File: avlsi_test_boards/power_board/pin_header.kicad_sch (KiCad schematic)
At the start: 61 parts, among them J5 Conn_02x20_Odd_Even, J6 Conn_02x20_Odd_Even, J7 Conn_02x20_Odd_Even, J8 Conn_02x20_Odd_Even, U11 SN74LVC16T245DLR, U12 SN74LVC16T245DLR, U13 SN74LVC16T245DLR, U14 SN74LVC16T245DLR, U17 SN74LVC16T245DLR, U18 SN74LVC16T245DLR, U19 SN74LVC16T245DLR

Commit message: Fully routed
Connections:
- net VIN is gone; now on net V_Level_Shift: S1.A2, S1.B2, S2.A2, S2.B2, S3.A2, S3.B2, S4.A2, S4.B2, S5.A2, S5.B2, S6.A2, S6.B2, S7.A2, S7.B2
- net DGND: now also C10.1, C11.1, C12.1, C13.1, C14.1, C15.1, C16.1, C19.1, C20.1, C23.1, C24.1, C25.1, C26.1, C27.1, C28.1, C29.1, C30.1, C35.1, C36.1, C38.1, C39.1, C40.1, C41.1, C43.1, C44.1, C45.1, C6.1, C9.1, R1.2, R10.2, R11.2, R12.2, R13.2, R14.2, R2.2, R3.2, R4.2, R5.2, R6.2, R7.2, R8.2, R9.2, U11.10 (GND), U11.15 (GND), U11.21 (GND), U11.28 (GND), U11.34 (GND), U11.39 (GND), U11.4 (GND), U11.45 (GND), U12.10 (GND), U12.15 (GND), U12.21 (GND), U12.28 (GND), U12.34 (GND), U12.39 (GND), U12.4 (GND), U12.45 (GND), U13.10 (GND), U13.15 (GND), U13.21 (GND), U13.28 (GND), U13.34 (GND), U13.39 (GND), U13.4 (GND), U13.45 (GND), U14.10 (GND), U14.15 (GND), U14.21 (GND), U14.28 (GND), U14.34 (GND), U14.39 (GND), U14.4 (GND), U14.45 (GND), U17.10 (GND), U17.15 (GND), U17.21 (GND), U17.28 (GND), U17.34 (GND), U17.39 (GND), U17.4 (GND), U17.45 (GND), U18.10 (GND), U18.15 (GND), U18.21 (GND), U18.28 (GND), U18.34 (GND), U18.39 (GND), U18.4 (GND), U18.45 (GND), U19.10 (GND), U19.15 (GND), U19.21 (GND), U19.28 (GND), U19.34 (GND), U19.39 (GND), U19.4 (GND), U19.45 (GND)
- net DIR1_6: now also R4.1
- net HA1: now also J5.36 (Pin_36); no longer J5.35 (Pin_35)
- net HA10: now also J5.27 (Pin_27); no longer J5.28 (Pin_28)
- net HA11: now also J5.26 (Pin_26); no longer J5.25 (Pin_25)
- net HA12: now also J5.25 (Pin_25); no longer J5.26 (Pin_26)
- net HA13: now also J5.24 (Pin_24); no longer J5.23 (Pin_23)
- net HA14: now also J5.23 (Pin_23); no longer J5.24 (Pin_24)
- net HA15: now also J5.22 (Pin_22); no longer J5.21 (Pin_21)
- net HA16: now also J5.21 (Pin_21); no longer J5.22 (Pin_22)
- net HA2: now also J5.35 (Pin_35); no longer J5.36 (Pin_36)
- net HA3: now also J5.34 (Pin_34); no longer J5.33 (Pin_33)
- net HA4: now also J5.33 (Pin_33); no longer J5.34 (Pin_34)
- net HA5: now also J5.32 (Pin_32); no longer J5.31 (Pin_31)
- net HA6: now also J5.31 (Pin_31); no longer J5.32 (Pin_32)
- net HA7: now also J5.30 (Pin_30); no longer J5.29 (Pin_29)
- net HA8: now also J5.29 (Pin_29); no longer J5.30 (Pin_30)
- net HA9: now also J5.28 (Pin_28); no longer J5.27 (Pin_27)
- net HB1: now also J6.8 (Pin_8); no longer J6.7 (Pin_7)
- net HB11: now also J8.4 (Pin_4); no longer J8.3 (Pin_3)
- net HB12: now also J8.3 (Pin_3); no longer J8.4 (Pin_4)
- net HB13: now also J8.6 (Pin_6); no longer J8.5 (Pin_5)
- net HB14: now also J8.5 (Pin_5); no longer J8.6 (Pin_6)
- net HB15: now also J8.8 (Pin_8); no longer J8.7 (Pin_7)
- net HB16: now also J8.7 (Pin_7); no longer J8.8 (Pin_8)
- net HB2: now also J6.7 (Pin_7); no longer J6.8 (Pin_8)
- net HB3: now also J6.6 (Pin_6); no longer J6.5 (Pin_5)
- net HB4: now also J6.5 (Pin_5); no longer J6.6 (Pin_6)
- net HB5: now also J6.4 (Pin_4); no longer J6.3 (Pin_3)
- net HB6: now also J6.3 (Pin_3); no longer J6.4 (Pin_4)
- net HB7: now also J6.2 (Pin_2); no longer J6.1 (Pin_1)
- net HB8: now also J6.1 (Pin_1); no longer J6.2 (Pin_2)
- net HC6: now also U17.40 (1A6); no longer U17.39 (GND)
- net OPF1: now also J5.38 (Pin_38); no longer J5.37 (Pin_37)
- net OPH1: now also J5.37 (Pin_37); no longer J5.38 (Pin_38)
- net OPH2: now also J5.40 (Pin_40); no longer J5.39 (Pin_39)
- net OPH3: now also J5.39 (Pin_39); no longer J5.40 (Pin_40)
- removed net GND: C10.1, C11.1, C12.1, C13.1, C14.1, C15.1, C16.1, C19.1, C20.1, C23.1, C24.1, C25.1, C26.1, C27.1, C28.1, C29.1, C30.1, C35.1, C36.1, C38.1, C39.1, C40.1, C41.1, C43.1, C44.1, C45.1, C6.1, C9.1, R1.2, R10.2, R11.2, R12.2, R13.2, R14.2, R2.2, R3.2, R4.2, R5.2, R6.2, R7.2, R8.2, R9.2, U11.10 (GND), U11.15 (GND), U11.21 (GND), U11.28 (GND), U11.34 (GND), U11.39 (GND), U11.4 (GND), U11.45 (GND), U12.10 (GND), U12.15 (GND), U12.21 (GND), U12.28 (GND), U12.34 (GND), U12.39 (GND), U12.4 (GND), U12.45 (GND), U13.10 (GND), U13.15 (GND), U13.21 (GND), U13.28 (GND), U13.34 (GND), U13.39 (GND), U13.4 (GND), U13.45 (GND), U14.15 (GND), U14.21 (GND), U14.28 (GND), U14.34 (GND), U14.39 (GND), U14.4 (GND), U14.45 (GND), U17.15 (GND), U17.21 (GND), U17.28 (GND), U17.34 (GND), U17.4 (GND), U17.40 (1A6), U17.45 (GND), U18.10 (GND), U18.15 (GND), U18.21 (GND), U18.28 (GND), U18.34 (GND), U18.39 (GND), U18.4 (GND), U18.45 (GND), U19.10 (GND), U19.15 (GND), U19.21 (GND), U19.28 (GND), U19.34 (GND), U19.39 (GND), U19.4 (GND), U19.45 (GND)

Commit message: more changes
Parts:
- removed J7: Conn_02x20_Odd_Even, Connector_PinHeader_2.00mm:PinHeader_2x20_P2.00mm_Vertical, symbol Connector_Generic:Conn_02x20_Odd_Even
- added J4: Conn_02x10_Odd_Even, Connector_PinHeader_2.00mm:PinHeader_2x10_P2.00mm_Vertical, symbol Connector_Generic:Conn_02x10_Odd_Even
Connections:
- net 3VDD: now also J4.10 (Pin_10), J4.7 (Pin_7), J4.8 (Pin_8)
- net DGND: now also J4.1 (Pin_1), J4.15 (Pin_15), J4.2 (Pin_2), J4.3 (Pin_3), J4.4 (Pin_4), J4.6 (Pin_6), J4.9 (Pin_9)
- net FPGA_TCK: now also J4.11 (Pin_11)
- net FPGA_TDI: now also J4.13 (Pin_13)
- net FPGA_TDO: now also J4.5 (Pin_5)
- net FPGA_TMS: now also J4.14 (Pin_14)
- net OPB1: now also J4.20 (Pin_20)
- net OPD1: now also J4.19 (Pin_19)
- net SYS_CLK_MC2: now also J4.16 (Pin_16)
- net VCCBATT: now also J4.12 (Pin_12)
- net VCCO_MC2: now also J4.17 (Pin_17), J4.18 (Pin_18)

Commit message: Add partial changes
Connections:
- net DGND: now also U11.25 (*2OE), U11.48 (*1OE), U12.25 (*2OE), U12.48 (*1OE), U13.25 (*2OE), U13.48 (*1OE), U14.25 (*2OE), U17.25 (*2OE), U17.48 (*1OE), U18.25 (*2OE), U18.48 (*1OE), U19.25 (*2OE), U19.48 (*1OE)

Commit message: Add updated schematic
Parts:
- removed C10, C11, C12, C13, C14, C15, C16, C19, C20, C23, C24, C25, C26, C27, C28, C29, C30, C35, C36, C38, C39, C40, C41, C43, C44, C45, C6, C9: 1u, Capacitor_SMD:C_0603_1608Metric, symbol Device:C
- removed J4: Conn_02x10_Odd_Even, Connector_PinHeader_2.00mm:PinHeader_2x10_P2.00mm_Vertical, symbol Connector_Generic:Conn_02x10_Odd_Even
- removed R1, R10, R11, R12, R13, R14, R2, R3, R4, R5, R6, R7, R8, R9: 4.7k, Resistor_SMD:R_0201_0603Metric, symbol Device:R
- removed S1, S2, S3, S4, S5, S6, S7: 2454985-3, 24549853, symbol 2_DIP:2454985-3
- removed U11, U12, U13, U14, U17, U18, U19: SN74LVC16T245DLR, avlsi:DL48, symbol AVLSI:SN74LVC16T245DLR
- removed U2: ~, avlsi:opal_kelly_XEM7310_header, symbol AVLSI:opal_kelly_XEM7310_header
- added J7: Conn_02x20_Odd_Even, Connector_PinHeader_2.00mm:PinHeader_2x20_P2.00mm_Vertical, symbol Connector_Generic:Conn_02x20_Odd_Even
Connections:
- net 18VDD is gone; now on net FPGA_TCK: J5.6 (Pin_6)
- net HA1 is gone; now on net FPGA_33VDD: J5.36 (Pin_36)
- net HC7 is gone; now on net FPGA_GND: J8.16 (Pin_16)
- net HC8 is gone; now on net FPGA_33VDD: J8.15 (Pin_15)
- net HD14 is gone; now on net FPGA_GND: J8.37 (Pin_37)
- net HD16 is gone; now on net FPGA_GND: J8.39 (Pin_39)
- net HE13 is gone; now on net FPGA_GND: J6.37 (Pin_37)
- net HE15 is gone; now on net FPGA_GND: J6.39 (Pin_39)
- net HF7 is gone; now on net FPGA_GND: J6.15 (Pin_15)
- net HF8 is gone; now on net FPGA_33VDD: J6.16 (Pin_16)
- net FPGA_TDI: now also J5.10 (Pin_10)
- net FPGA_TDO: now also J5.7 (Pin_7)
- net FPGA_TMS: now also J5.8 (Pin_8)
- net SYS_CKL_MC1: now also J7.7 (Pin_7); no longer J5.13 (Pin_13)
- net SYS_CLK_MC2: now also J5.12 (Pin_12)
- net VCCBATT: now also J5.4 (Pin_4)
- net XADC_VN: now also J7.9 (Pin_9); no longer J5.14 (Pin_14)
- net XADC_VP: now also J7.11 (Pin_11); no longer J5.15 (Pin_15)
- net 10VDD renamed MC2_12
- net MC2_12: no longer J5.12 (Pin_12)
- net 33VDD renamed FPGA_33VDD
- net FPGA_33VDD: now also J5.1 (Pin_1), J7.10 (Pin_10), J7.12 (Pin_12), J7.14 (Pin_14), J7.35 (Pin_35); no longer J5.4 (Pin_4)
- removed net DGND: J5.1 (Pin_1), J5.10 (Pin_10), J5.16 (Pin_16), J5.19 (Pin_19), J5.2 (Pin_2), J5.20 (Pin_20)
- net HA10 renamed MC2_28_PIN
- net HA11 renamed MC2_25_PIN
- net HA12 renamed MC2_26_PIN
- net HA13 renamed MC2_23_PIN
- net HA14 renamed MC2_24
- net HA15 renamed MC2_21_PIN
- net HA16 renamed MC2_22
- net HA2 renamed FPGA_GND
- net FPGA_GND: now also J5.13 (Pin_13), J5.14 (Pin_14), J5.2 (Pin_2), J7.1 (Pin_1), J7.13 (Pin_13), J7.36 (Pin_36)
- net HA3 renamed MC2_33_PIN
- net HA4 renamed MC2_34_PIN
- net HA5 renamed MC2_31_PIN
- net HA6 renamed MC2_32_PIN
- net HA7 renamed MC2_29_PIN
- net HA8 renamed MC2_30_PIN
- net HA9 renamed MC2_27_PIN
- net HB1 renamed MC2_47_PIN
- net HB10 renamed MC1_42_PIN
- net HB11 renamed MC1_43_PIN
- net HB12 renamed MC1_44_PIN
- net HB13 renamed MC1_45_PIN
- net HB14 renamed MC1_46_PIN
- net HB15 renamed MC1_47_PIN
- net HB16 renamed MC1_48_PIN
- net HB2 renamed MC2_48_PIN
- net HB3 renamed MC2_45_PIN
- net HB4 renamed MC2_46_PIN
- net HB5 renamed MC2_43_PIN
- net HB6 renamed MC2_44_PIN
- net HB7 renamed MC2_41_PIN
- net HB8 renamed MC2_42_PIN
- net HB9 renamed MC1_41_PIN
- net HC1 renamed MC1_49_PIN
- net HC10 renamed MC1_58_PIN
- net HC11 renamed MC1_59_PIN
- net HC12 renamed MC1_60_PIN
- net HC13 renamed MC1_61_PIN
- net HC14 renamed MC1_62_PIN
- net HC15 renamed MC1_63_PIN
- net HC16 renamed MC1_64_PIN
- net HC2 renamed MC1_50_PIN
- net HC3 renamed MC1_51_PIN
- net HC4 renamed MC1_52_PIN
- net HC5 renamed MC1_53_PIN
- net HC6 renamed MC1_54_PIN
- net HC9 renamed MC1_57_PIN
- net HD1 renamed MC1_65_PIN
- net HD10 renamed MC1_74_PIN
- net HD11 renamed MC1_75
- net HD12 renamed MC1_76_PIN
- net HD13 renamed MC1_77
- net HD15 renamed MC1_79
- net HD2 renamed MC1_66_PIN
- net HD3 renamed MC1_67_PIN
- net HD4 renamed MC1_68_PIN
- net HD5 renamed MC1_69_PIN
- net HD6 renamed MC1_70_PIN
- net HD7 renamed MC1_71_PIN
- net HD8 renamed MC1_72_PIN
- net HD9 renamed MC1_73
- net HE1 renamed MC2_66_PIN
- net HE10 renamed MC2_73_PIN
- net HE11 renamed MC2_76_PIN
- net HE12 renamed MC2_75_PIN
- net HE14 renamed MC2_77_PIN
- net HE16 renamed MC2_79_PIN
- net HE2 renamed MC2_65_PIN
- net HE3 renamed MC2_68_PIN
- net HE4 renamed MC2_67_PIN
- net HE5 renamed MC2_70_PIN
- net HE6 renamed MC2_69_PIN
- net HE7 renamed MC2_72_PIN
- net HE8 renamed MC2_71_PIN
- net HE9 renamed MC2_74_PIN
- net HF1 renamed MC2_50_PIN
- net HF10 renamed MC2_57_PIN
- net HF11 renamed MC2_60_PIN
- net HF12 renamed MC2_59_PIN
- net HF13 renamed MC2_62_PIN
- net HF14 renamed MC2_61_PIN
- net HF15 renamed MC2_64_PIN
- net HF16 renamed MC2_63_PIN
- net HF2 renamed MC2_49_PIN
- net HF3 renamed MC2_52_PIN
- net HF4 renamed MC2_51_PIN
- net HF5 renamed MC2_54_PIN
- net HF6 renamed MC2_53_PIN
- net HF9 renamed MC2_58_PIN
- net OPF1 renamed MC2_37_PIN
- net OPH1 renamed MC2_38_PIN
- net OPH2 renamed MC2_39_PIN
- net OPH3 renamed MC2_40_PIN
- net VCCO_MC1 renamed MC2_17_PIN
- net MC2_17_PIN: no longer J5.17 (Pin_17)
- removed net VDCIN: J5.7 (Pin_7), J5.8 (Pin_8), J5.9 (Pin_9)
- new net FPGA_10VDD: J7.3 (Pin_3), J7.5 (Pin_5)
- new net FPGA_18VDD: J7.8 (Pin_8)
- new net FPGA_VCDIN: J7.2 (Pin_2), J7.4 (Pin_4), J7.6 (Pin_6)
- new net MC1_15_PIN: J7.16 (Pin_16)
- new net MC1_16_PIN: J7.15 (Pin_15)
- new net MC1_17_PIN: J7.18 (Pin_18)
- new net MC1_18_PIN: J7.17 (Pin_17)
- new net MC1_19_PIN: J7.20 (Pin_20)
- new net MC1_20_PIN: J7.19 (Pin_19)
- new net MC1_21_PIN: J7.22 (Pin_22)
- new net MC1_22_PIN: J7.21 (Pin_21)
- new net MC1_23_PIN: J7.24 (Pin_24)
- new net MC1_24_PIN: J7.23 (Pin_23)
- new net MC1_25_PIN: J7.26 (Pin_26)
- new net MC1_26_PIN: J7.25 (Pin_25)
- new net MC1_27_PIN: J7.28 (Pin_28)
- new net MC1_28_PIN: J7.27 (Pin_27)
- new net MC1_29_PIN: J7.30 (Pin_30)
- new net MC1_30_PIN: J7.29 (Pin_29)
- new net MC1_31_PIN: J7.32 (Pin_32)
- new net MC1_32_PIN: J7.31 (Pin_31)
- new net MC1_33_PIN: J7.34 (Pin_34)
- new net MC1_34_PIN: J7.33 (Pin_33)
- new net MC1_37_PIN: J7.38 (Pin_38)
- new net MC1_38_PIN: J7.37 (Pin_37)
- new net MC1_39_PIN: J7.40 (Pin_40)
- new net MC1_40_PIN: J7.39 (Pin_39)
- new net MC2_10_PIN: J5.9 (Pin_9)
- new net MC2_15_PIN: J5.16 (Pin_16)
- new net MC2_16: J5.15 (Pin_15)
- new net MC2_18: J5.17 (Pin_17)
- new net MC2_19_PIN: J5.20 (Pin_20)
- new net MC2_20: J5.19 (Pin_19)
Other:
- note removed: "1 extra pad"
- note removed: "3 extra pads"
- note removed: "Near analog power, empty pins are open"
- note removed: "On back copper"
- note removed: "This side up"
- moved on the sheet: J6

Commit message: Add fix typo
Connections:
- net SYS_CKL_MC1 renamed SYS_CLK_MC1
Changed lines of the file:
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@@
 		)
 	)
-	(global_label "SYS_CKL_MC1"
+	(global_label "SYS_CLK_MC1"
 		(shape input)
 		(at 222.25 40.64 180)

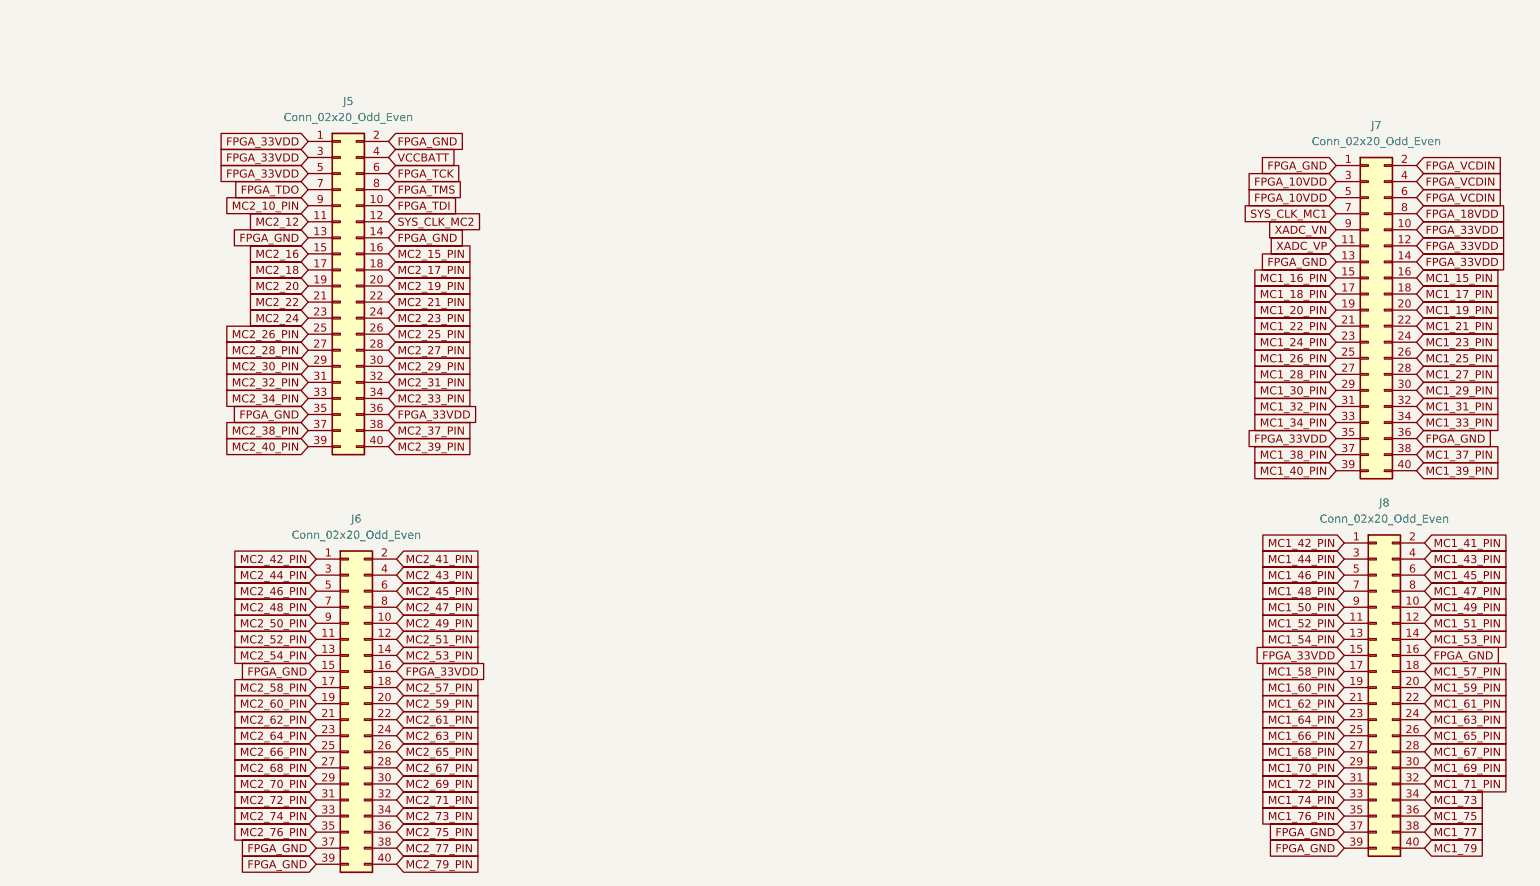
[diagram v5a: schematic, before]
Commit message: Update schematic and initial layout for pcb
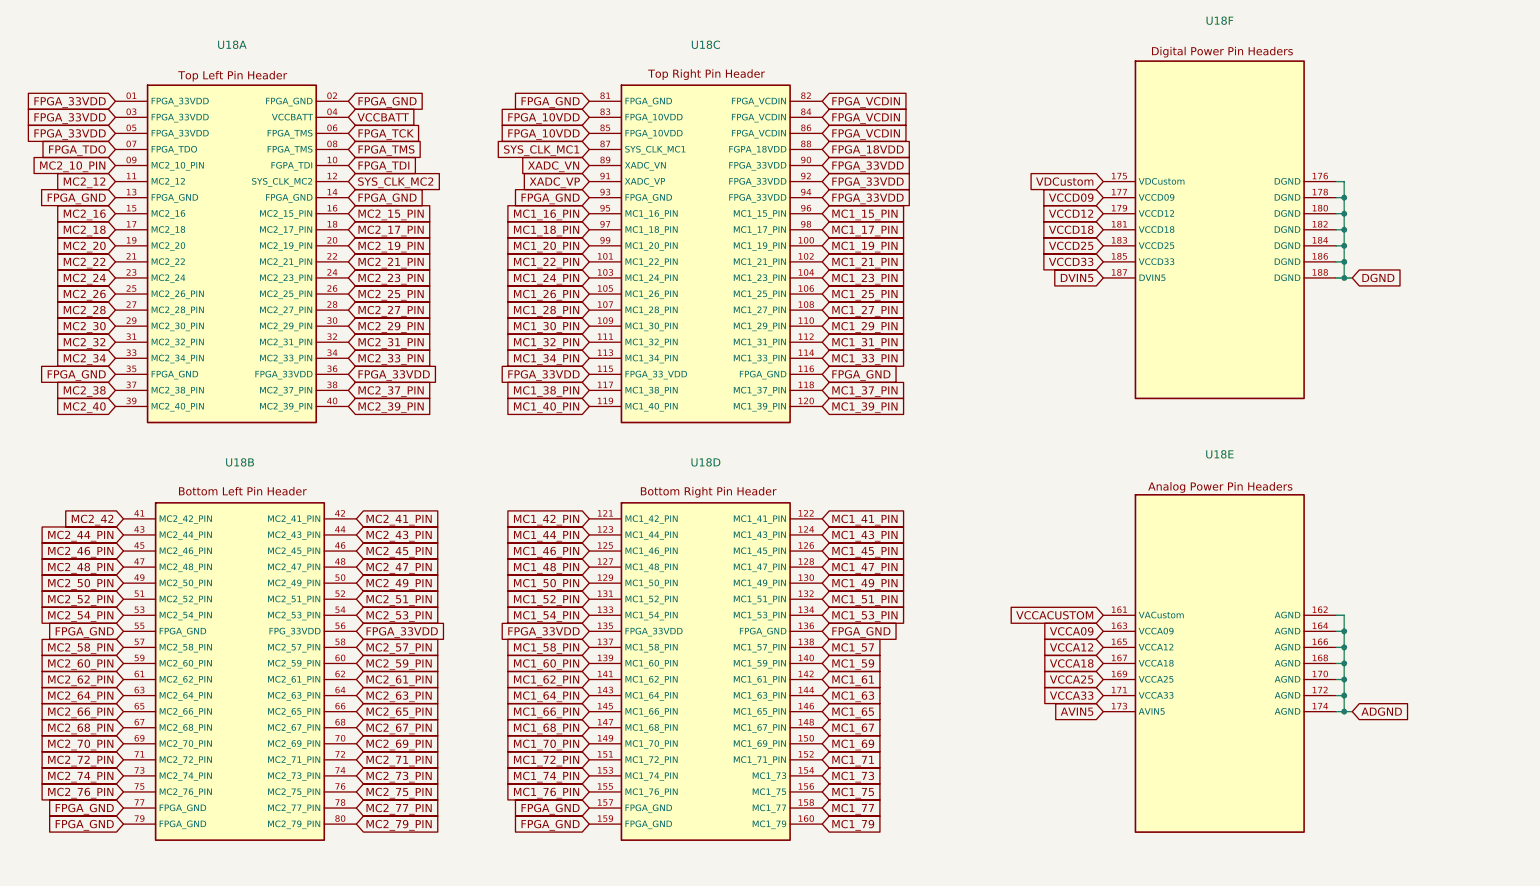
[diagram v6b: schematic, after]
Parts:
- removed J5, J6, J7, J8: Conn_02x20_Odd_Even, Connector_PinHeader_2.00mm:PinHeader_2x20_P2.00mm_Vertical, symbol Connector_Generic:Conn_02x20_Odd_Even
- added U18: ~, avlsi_preferred_parts:avlsi_power_board_opal_kelly, symbol avlsi_preferred_parts:avlsi_power_board_opal_kelly
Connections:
- net FPGA_10VDD: now also U18.83 (FPGA_10VDD), U18.85 (FPGA_10VDD)
- net FPGA_18VDD: now also U18.88 (FGPA_18VDD)
- net FPGA_33VDD: now also U18.01 (FPGA_33VDD), U18.03 (FPGA_33VDD), U18.05 (FPGA_33VDD), U18.115 (FPGA_33_VDD), U18.135 (FPGA_33VDD), U18.36 (FPGA_33VDD), U18.56 (FPG_33VDD), U18.90 (FPGA_33VDD), U18.92 (FPGA_33VDD), U18.94 (FPGA_33VDD)
- net FPGA_GND: now also U18.02 (FPGA_GND), U18.116 (FPGA_GND), U18.13 (FPGA_GND), U18.136 (FPGA_GND), U18.14 (FPGA_GND), U18.157 (FPGA_GND), U18.159 (FPGA_GND), U18.35 (FPGA_GND), U18.55 (FPGA_GND), U18.77 (FPGA_GND), U18.79 (FPGA_GND), U18.81 (FPGA_GND), U18.93 (FPGA_GND)
- net FPGA_TCK: now also U18.06 (FPGA_TMS)
- net FPGA_TDI: now also U18.10 (FGPA_TDI)
- net FPGA_TDO: now also U18.07 (FPGA_TDO)
- net FPGA_TMS: now also U18.08 (FPGA_TMS)
- net FPGA_VCDIN: now also U18.82 (FPGA_VCDIN), U18.84 (FPGA_VCDIN), U18.86 (FPGA_VCDIN)
- net MC1_15_PIN: now also U18.96 (MC1_15_PIN)
- net MC1_16_PIN: now also U18.95 (MC1_16_PIN)
- net MC1_17_PIN: now also U18.98 (MC1_17_PIN)
- net MC1_18_PIN: now also U18.97 (MC1_18_PIN)
- net MC1_19_PIN: now also U18.100 (MC1_19_PIN)
- net MC1_20_PIN: now also U18.99 (MC1_20_PIN)
- net MC1_21_PIN: now also U18.102 (MC1_21_PIN)
- net MC1_22_PIN: now also U18.101 (MC1_22_PIN)
- net MC1_23_PIN: now also U18.104 (MC1_23_PIN)
- net MC1_24_PIN: now also U18.103 (MC1_24_PIN)
- net MC1_25_PIN: now also U18.106 (MC1_25_PIN)
- net MC1_26_PIN: now also U18.105 (MC1_26_PIN)
- net MC1_27_PIN: now also U18.108 (MC1_27_PIN)
- net MC1_28_PIN: now also U18.107 (MC1_28_PIN)
- net MC1_29_PIN: now also U18.110 (MC1_29_PIN)
- net MC1_30_PIN: now also U18.109 (MC1_30_PIN)
- net MC1_31_PIN: now also U18.112 (MC1_31_PIN)
- net MC1_32_PIN: now also U18.111 (MC1_32_PIN)
- net MC1_33_PIN: now also U18.114 (MC1_33_PIN)
- net MC1_34_PIN: now also U18.113 (MC1_34_PIN)
- net MC1_37_PIN: now also U18.118 (MC1_37_PIN)
- net MC1_38_PIN: now also U18.117 (MC1_38_PIN)
- net MC1_39_PIN: now also U18.120 (MC1_39_PIN)
- net MC1_40_PIN: now also U18.119 (MC1_40_PIN)
- net MC1_41_PIN: now also U18.122 (MC1_41_PIN)
- net MC1_42_PIN: now also U18.121 (MC1_42_PIN)
- net MC1_43_PIN: now also U18.124 (MC1_43_PIN)
- net MC1_44_PIN: now also U18.123 (MC1_44_PIN)
- net MC1_45_PIN: now also U18.126 (MC1_45_PIN)
- net MC1_46_PIN: now also U18.125 (MC1_46_PIN)
- net MC1_47_PIN: now also U18.128 (MC1_47_PIN)
- net MC1_48_PIN: now also U18.127 (MC1_48_PIN)
- net MC1_49_PIN: now also U18.130 (MC1_49_PIN)
- net MC1_50_PIN: now also U18.129 (MC1_50_PIN)
- net MC1_51_PIN: now also U18.132 (MC1_51_PIN)
- net MC1_52_PIN: now also U18.131 (MC1_52_PIN)
- net MC1_53_PIN: now also U18.134 (MC1_53_PIN)
- net MC1_54_PIN: now also U18.133 (MC1_54_PIN)
- net MC1_58_PIN: now also U18.137 (MC1_58_PIN)
- net MC1_60_PIN: now also U18.139 (MC1_60_PIN)
- net MC1_62_PIN: now also U18.141 (MC1_62_PIN)
- net MC1_64_PIN: now also U18.143 (MC1_64_PIN)
- net MC1_66_PIN: now also U18.145 (MC1_66_PIN)
- net MC1_68_PIN: now also U18.147 (MC1_68_PIN)
- net MC1_70_PIN: now also U18.149 (MC1_70_PIN)
- net MC1_72_PIN: now also U18.151 (MC1_72_PIN)
- net MC1_73: now also U18.154 (MC1_73)
- net MC1_74_PIN: now also U18.153 (MC1_74_PIN)
- net MC1_75: now also U18.156 (MC1_75)
- net MC1_76_PIN: now also U18.155 (MC1_76_PIN)
- net MC1_77: now also U18.158 (MC1_77)
- net MC1_79: now also U18.160 (MC1_79)
- net MC2_10_PIN: now also U18.09 (MC2_10_PIN)
- net MC2_12: now also U18.11 (MC2_12)
- net MC2_15_PIN: now also U18.16 (MC2_15_PIN)
- net MC2_16: now also U18.15 (MC2_16)
- net MC2_17_PIN: now also U18.18 (MC2_17_PIN)
- net MC2_18: now also U18.17 (MC2_18)
- net MC2_19_PIN: now also U18.20 (MC2_19_PIN)
- net MC2_20: now also U18.19 (MC2_20)
- net MC2_21_PIN: now also U18.22 (MC2_21_PIN)
- net MC2_22: now also U18.21 (MC2_22)
- net MC2_23_PIN: now also U18.24 (MC2_23_PIN)
- net MC2_24: now also U18.23 (MC2_24)
- net MC2_25_PIN: now also U18.26 (MC2_25_PIN)
- net MC2_27_PIN: now also U18.28 (MC2_27_PIN)
- net MC2_29_PIN: now also U18.30 (MC2_29_PIN)
- net MC2_31_PIN: now also U18.32 (MC2_31_PIN)
- net MC2_33_PIN: now also U18.34 (MC2_33_PIN)
- net MC2_37_PIN: now also U18.38 (MC2_37_PIN)
- net MC2_39_PIN: now also U18.40 (MC2_39_PIN)
- net MC2_41_PIN: now also U18.42 (MC2_41_PIN)
- net MC2_43_PIN: now also U18.44 (MC2_43_PIN)
- net MC2_44_PIN: now also U18.43 (MC2_44_PIN)
- net MC2_45_PIN: now also U18.46 (MC2_45_PIN)
- net MC2_46_PIN: now also U18.45 (MC2_46_PIN)
- net MC2_47_PIN: now also U18.48 (MC2_47_PIN)
- net MC2_48_PIN: now also U18.47 (MC2_48_PIN)
- net MC2_49_PIN: now also U18.50 (MC2_49_PIN)
- net MC2_50_PIN: now also U18.49 (MC2_50_PIN)
- net MC2_51_PIN: now also U18.52 (MC2_51_PIN)
- net MC2_52_PIN: now also U18.51 (MC2_52_PIN)
- net MC2_53_PIN: now also U18.54 (MC2_53_PIN)
- net MC2_54_PIN: now also U18.53 (MC2_54_PIN)
- net MC2_57_PIN: now also U18.58 (MC2_57_PIN)
- net MC2_58_PIN: now also U18.57 (MC2_58_PIN)
- net MC2_59_PIN: now also U18.60 (MC2_59_PIN)
- net MC2_60_PIN: now also U18.59 (MC2_60_PIN)
- net MC2_61_PIN: now also U18.62 (MC2_61_PIN)
- net MC2_62_PIN: now also U18.61 (MC2_62_PIN)
- net MC2_63_PIN: now also U18.64 (MC2_63_PIN)
- net MC2_64_PIN: now also U18.63 (MC2_64_PIN)
- net MC2_65_PIN: now also U18.66 (MC2_65_PIN)
- net MC2_66_PIN: now also U18.65 (MC2_66_PIN)
- net MC2_67_PIN: now also U18.68 (MC2_67_PIN)
- net MC2_68_PIN: now also U18.67 (MC2_68_PIN)
- net MC2_69_PIN: now also U18.70 (MC2_69_PIN)
- net MC2_70_PIN: now also U18.69 (MC2_70_PIN)
- net MC2_71_PIN: now also U18.72 (MC2_71_PIN)
- net MC2_72_PIN: now also U18.71 (MC2_72_PIN)
- net MC2_73_PIN: now also U18.74 (MC2_73_PIN)
- net MC2_74_PIN: now also U18.73 (MC2_74_PIN)
- net MC2_75_PIN: now also U18.76 (MC2_75_PIN)
- net MC2_76_PIN: now also U18.75 (MC2_76_PIN)
- net MC2_77_PIN: now also U18.78 (MC2_77_PIN)
- net MC2_79_PIN: now also U18.80 (MC2_79_PIN)
- net SYS_CLK_MC1: now also U18.87 (SYS_CLK_MC1)
- net SYS_CLK_MC2: now also U18.12 (SYS_CLK_MC2)
- net VCCBATT: now also U18.04 (VCCBATT)
- net XADC_VN: now also U18.89 (XADC_VN)
- net XADC_VP: now also U18.91 (XADC_VP)
- new net ADGND: U18.162 (AGND), U18.164 (AGND), U18.166 (AGND), U18.168 (AGND), U18.170 (AGND), U18.172 (AGND), U18.174 (AGND)
- new net AVIN5: U18.173 (AVIN5)
- new net DGND: U18.176 (DGND), U18.178 (DGND), U18.180 (DGND), U18.182 (DGND), U18.184 (DGND), U18.186 (DGND), U18.188 (DGND)
- new net DVIN5: U18.187 (DVIN5)
- new net MC1_57: U18.138 (MC1_57_PIN)
- new net MC1_59: U18.140 (MC1_59_PIN)
- new net MC1_61: U18.142 (MC1_61_PIN)
- new net MC1_63: U18.144 (MC1_63_PIN)
- new net MC1_65: U18.146 (MC1_65_PIN)
- new net MC1_67: U18.148 (MC1_67_PIN)
- new net MC1_69: U18.150 (MC1_69_PIN)
- new net MC1_71: U18.152 (MC1_71_PIN)
- new net MC2_26: U18.25 (MC2_26_PIN)
- new net MC2_28: U18.27 (MC2_28_PIN)
- new net MC2_30: U18.29 (MC2_30_PIN)
- new net MC2_32: U18.31 (MC2_32_PIN)
- new net MC2_34: U18.33 (MC2_34_PIN)
- new net MC2_38: U18.37 (MC2_38_PIN)
- new net MC2_40: U18.39 (MC2_40_PIN)
- new net MC2_42: U18.41 (MC2_42_PIN)
- new net VCCA09: U18.163 (VCCA09)
- new net VCCA12: U18.165 (VCCA12)
- new net VCCA18: U18.167 (VCCA18)
- new net VCCA25: U18.169 (VCCA25)
- new net VCCA33: U18.171 (VCCA33)
- new net VCCACUSTOM: U18.161 (VACustom)
- new net VCCD09: U18.177 (VCCD09)
- new net VCCD12: U18.179 (VCCD12)
- new net VCCD18: U18.181 (VCCD18)
- new net VCCD25: U18.183 (VCCD25)
- new net VCCD33: U18.185 (VCCD33)
- new net VDCustom: U18.175 (VDCustom)
